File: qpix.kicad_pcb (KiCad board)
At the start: 2 copper layers, 82.6 x 93 mm, 113 parts, among them J1 Conn_01x32, J11 Conn_Coaxial_Power, J12 USB_A, J13 DigReset, J2 Conn_01x09, J3 TxRx_D, J4 TxRx_A, J5 SPI, J6 TxRx_B, J7 Conn_Coaxial, J8 TxRx_C, J9 Conn_Coaxial_Power, Q1 Q, Q2 Q, Q3 Q, Q4 Q, U1 qpix_digital, U2 TPS73101DBV, U3 9DMV0141AKILF, U4 DS90C401M_NOPB

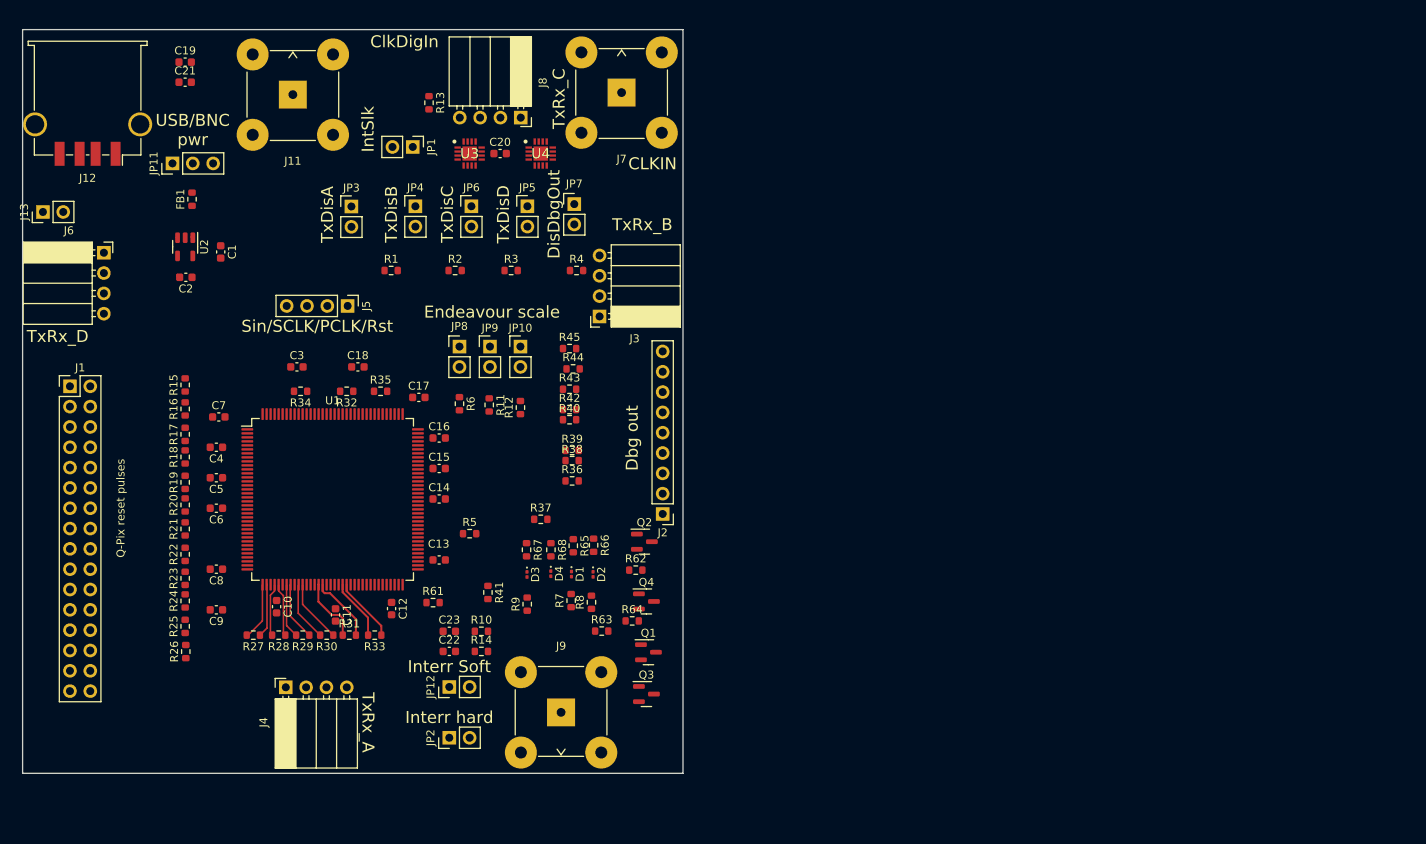
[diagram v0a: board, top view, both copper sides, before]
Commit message: add a footprint for QPix ASIC CoB  and its generator
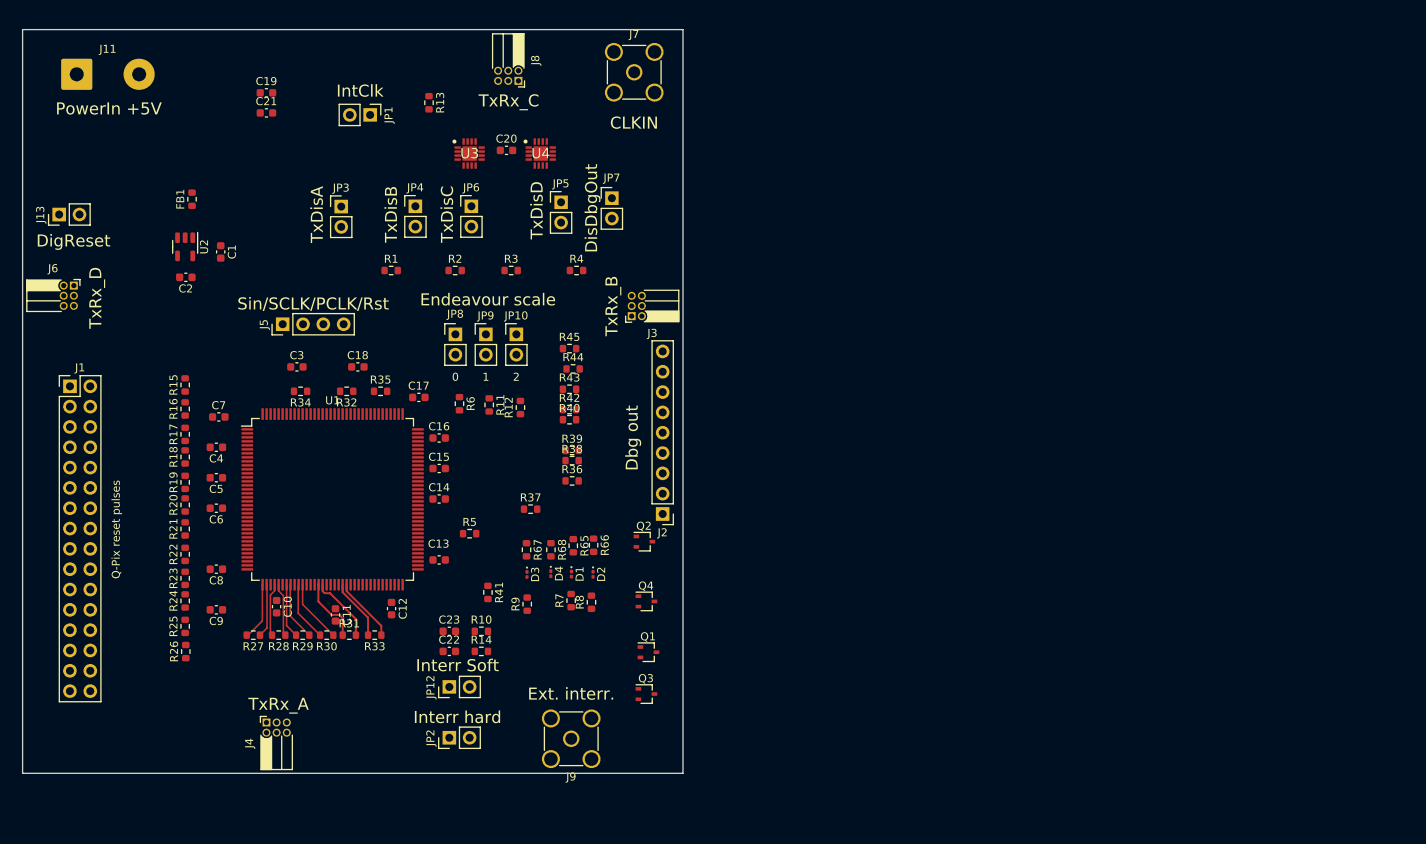
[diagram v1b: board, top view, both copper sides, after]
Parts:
- removed J12: USB_A, Connector_USB:USB_A_TE_292303-7_Horizontal
- removed JP11: , Connector_PinHeader_2.54mm:PinHeader_1x03_P2.54mm_Vertical
- removed R61, R62, R63, R64: 2.2k, Resistor_SMD:R_0603_1608Metric
- J11: footprint Connector_Coaxial:BNC_TEConnectivity_1478035_Horizontal -> Connector_Wire:SolderWire-1sqmm_1x02_P7.8mm_D1.4mm_OD3.9mm
- J3: value TxRx_D -> Conn_02x03; footprint Connector_PinSocket_2.54mm:PinSocket_1x04_P2.54mm_Horizontal -> Connector_PinSocket_1.27mm:PinSocket_2x03_P1.27mm_Horizontal
- J4: value TxRx_A -> Conn_02x03; footprint Connector_PinSocket_2.54mm:PinSocket_1x04_P2.54mm_Horizontal -> Connector_PinSocket_1.27mm:PinSocket_2x03_P1.27mm_Horizontal
- J6: value TxRx_B -> Conn_02x03; footprint Connector_PinSocket_2.54mm:PinSocket_1x04_P2.54mm_Horizontal -> Connector_PinSocket_1.27mm:PinSocket_2x03_P1.27mm_Horizontal
- J7, J9: footprint Connector_Coaxial:BNC_TEConnectivity_1478035_Horizontal -> Connector_Coaxial:SMA_Amphenol_901-144_Vertical
- J8: value TxRx_C -> Conn_02x03; footprint Connector_PinSocket_2.54mm:PinSocket_1x04_P2.54mm_Horizontal -> Connector_PinSocket_1.27mm:PinSocket_2x03_P1.27mm_Horizontal
- Q1, Q2, Q3, Q4: value Q -> Q_NMOS_GSD; footprint Package_TO_SOT_SMD:SOT-23 -> Package_TO_SOT_SMD:SOT-323_SC-70
- moved J11 27.1 mm to (102.0, 54.9)
- moved C19 10.9 mm to (125.7, 57.2)
- moved C21 10.9 mm to (125.7, 59.7)
- moved J5 8.43 mm to (127.8, 86.1), turned to 90 degrees
- moved JP1 6.66 mm to (138.7, 59.9)
- moved J6 5.56 mm to (101.7, 81.3)
- moved J4 5.02 mm to (125.7, 135.9)
- moved JP7 4.76 mm to (168.9, 70.4)
- moved J8 4.60 mm to (157.2, 55.7)
- moved JP5 4.24 mm to (162.6, 70.9)
- moved J3 4.02 mm to (171.4, 85.1)
- moved J9 3.54 mm to (163.8, 137.9)
- moved J7 2.99 mm to (171.7, 54.6)
- moved J13 2.06 mm to (99.8, 72.4)
- moved R37 1.80 mm to (158.8, 109.2)
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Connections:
- J11 pad 1: Net-(J11-Pad1) -> Net-(FB1-Pad2)
- J3 pad 2: Net-(J3-Pad2) -> Net-(U1-Pad106)
- J3 pad 3: Net-(J3-Pad3) -> GND
- J3 pad 4: Net-(J3-Pad4) -> GND
- J4 pad 2: Net-(J4-Pad2) -> Net-(U1-Pad54)
- J4 pad 3: Net-(J4-Pad3) -> GND
- J4 pad 4: Net-(J4-Pad4) -> GND
- J6 pad 2: Net-(J6-Pad2) -> Net-(U1-Pad62)
- J6 pad 3: Net-(J6-Pad3) -> GND
- J6 pad 4: Net-(J6-Pad4) -> GND
- J8 pad 2: Net-(J8-Pad2) -> Net-(U1-Pad101)
- J8 pad 3: Net-(J8-Pad3) -> GND
- J8 pad 4: Net-(J8-Pad4) -> GND
- Q1 pad 1: Net-(D1-Pad1) -> dbgClkDiv
- Q1 pad 2: Net-(R61-Pad2) -> GND
- Q1 pad 3: GND -> Net-(D1-Pad1)
- Q2 pad 1: Net-(D2-Pad1) -> dbgDataValid
- Q2 pad 2: Net-(Q2-Pad2) -> GND
- Q2 pad 3: GND -> Net-(D2-Pad1)
- Q3 pad 1: Net-(D3-Pad1) -> dbgRxValid
- Q3 pad 2: Net-(Q3-Pad2) -> GND
- Q3 pad 3: GND -> Net-(D3-Pad1)
- Q4 pad 1: Net-(D4-Pad1) -> dbgInterr
- Q4 pad 2: Net-(Q4-Pad2) -> GND
- Q4 pad 3: GND -> Net-(D4-Pad1)
- R31 pad 2: Net-(J4-Pad2) -> Net-(R31-Pad2)
- R32 pad 2: Net-(J3-Pad2) -> Net-(R32-Pad2)
- R33 pad 1: Net-(J6-Pad2) -> Net-(R33-Pad1)
- R35 pad 1: Net-(J8-Pad2) -> Net-(R35-Pad1)
- U1 pad 101: Net-(J8-Pad3) -> Net-(U1-Pad101)
- U1 pad 102: Net-(J8-Pad4) -> Net-(U1-Pad102)
- U1 pad 106: Net-(J3-Pad3) -> Net-(U1-Pad106)
- U1 pad 107: Net-(J3-Pad4) -> Net-(U1-Pad107)
- U1 pad 110: Net-(J3-Pad2) -> Net-(R32-Pad2)
- U1 pad 52: Net-(J4-Pad2) -> Net-(R31-Pad2)
- U1 pad 53: Net-(J4-Pad4) -> Net-(U1-Pad53)
- U1 pad 54: Net-(J4-Pad3) -> Net-(U1-Pad54)
- U1 pad 58: Net-(J6-Pad2) -> Net-(R33-Pad1)
- U1 pad 61: Net-(J6-Pad4) -> Net-(U1-Pad61)
- U1 pad 62: Net-(J6-Pad3) -> Net-(U1-Pad62)
- U1 pad 98: Net-(J8-Pad2) -> Net-(R35-Pad1)
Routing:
- net Net-(R31-Pad2): track 0.00 -> 8.42 mm
- net Net-(J4-Pad2): track 8.42 -> 0.00 mm
- net Net-(R33-Pad1): track 0.00 -> 8.10 mm
- net Net-(J6-Pad2): track 8.10 -> 0.00 mm
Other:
- board text added: "0"
- board text added: "1"
- board text added: "2"
- board text added: "DigReset"
- board text added: "Ext. interr."
- board text added: "IntClk"
- board text added: "PowerIn +5V"
- board text removed: "ClkDigIn"
- board text removed: "IntSlk"
- board text removed: "USB/BNC pwr"

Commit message: some changes
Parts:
- U1: footprint Package_QFP:TQFP-144_20x20mm_P0.5mm -> qpix-digi-pcb:qpix_digi_footprint
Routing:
- net (no net): track 0.00 -> 3.53 mm

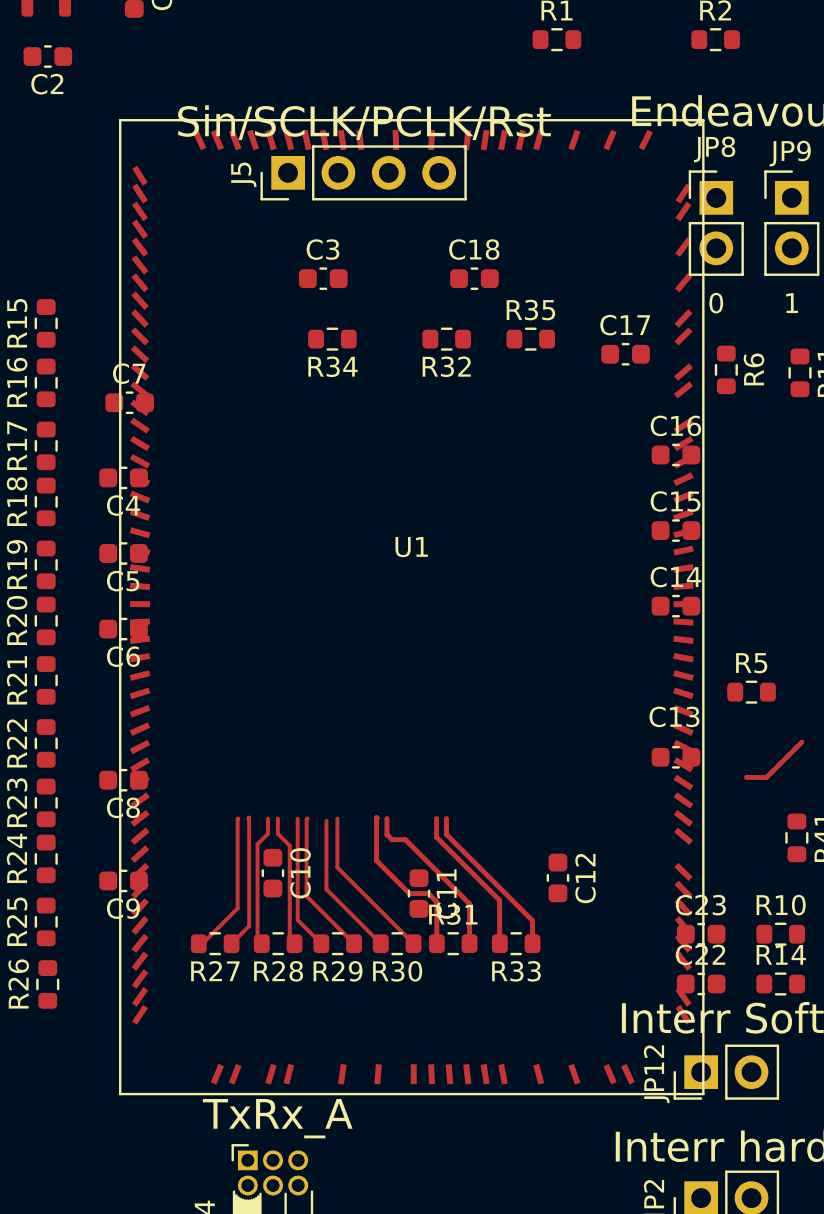
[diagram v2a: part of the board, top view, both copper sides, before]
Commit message: modify qpix footprint
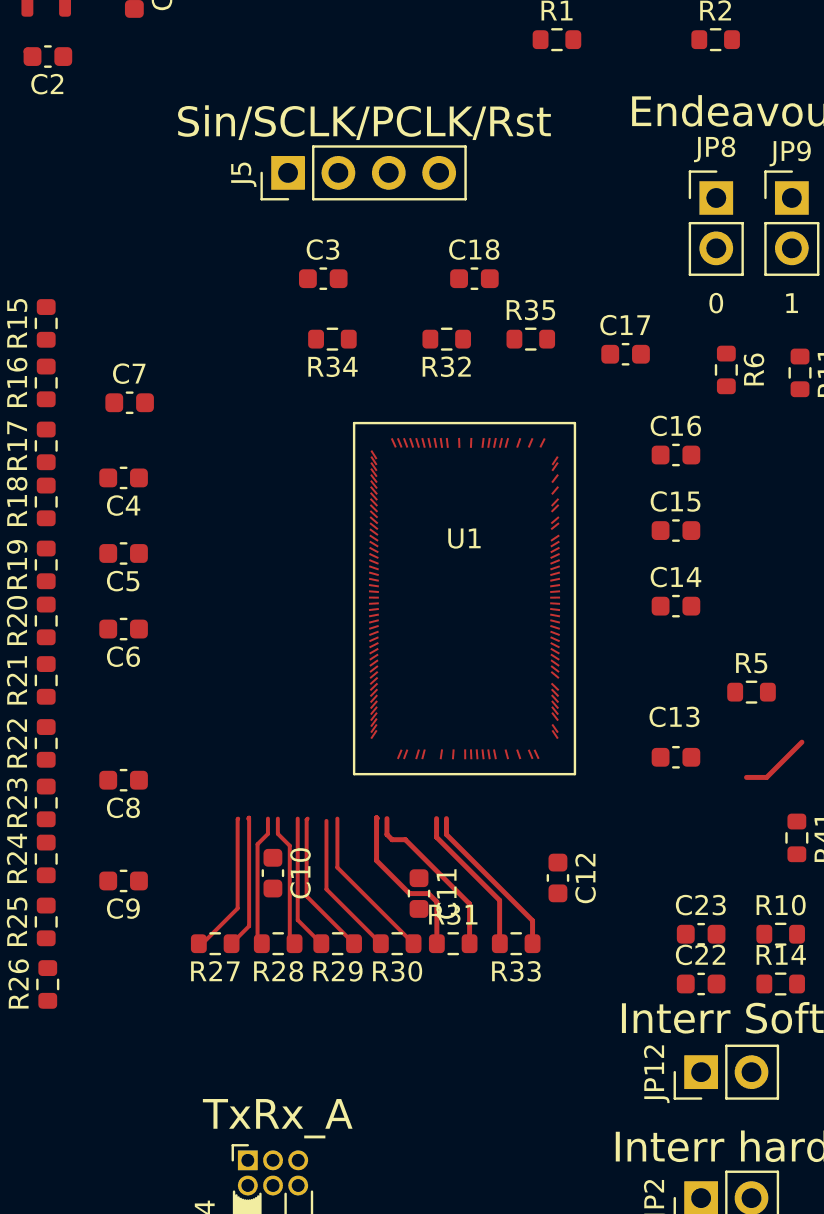
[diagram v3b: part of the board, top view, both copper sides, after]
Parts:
- moved U1 2.69 mm to (136.7, 107.6)

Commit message: some progress in routing
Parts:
- C12, C13, C14, C15, C16, C17, C18, C4, C5, C6, C7, C8, C9, R11, R12, R5, R6: moved to B.Cu
- moved D2 95.9 mm to (261.6, 129.9)
- moved R65 95.9 mm to (259.1, 126.4)
- moved R67 95.9 mm to (253.3, 126.9)
- moved D1 95.9 mm to (258.9, 129.9)
- moved D3 95.9 mm to (253.3, 130.0)
- moved D4 95.9 mm to (256.3, 129.9)
- moved R66 95.9 mm to (261.7, 126.3)
- moved R68 95.9 mm to (256.3, 126.9)
- moved Q1 94.0 mm to (267.4, 131.0)
- moved Q2 94.0 mm to (266.9, 117.2)
- moved Q3 94.0 mm to (267.1, 136.2)
- moved Q4 94.0 mm to (267.1, 124.6)
- moved R7 79.1 mm to (109.5, 63.1)
- moved R8 77.7 mm to (112.8, 64.5), turned to 0 degrees
- moved R9 71.5 mm to (115.8, 63.6)
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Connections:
- net Net-(JP1-Pad1) renamed /clkmux/SEL_AB
- net Net-(R31-Pad1) renamed /DatinA_P
- net Net-(R31-Pad2) renamed /DatinA_N
- net Net-(R33-Pad2) renamed /DatinB_P
- net Net-(U1-Pad53) renamed /DatoutA_N
- net Net-(U1-Pad54) renamed /DatoutA_P
- net Net-(U3-Pad15) renamed /clkmux/DO+
- net Net-(U3-Pad16) renamed /clkmux/DO-
- J6 pad 2: Net-(U1-Pad62) -> /DatinB_N
- J6 pad 5: Net-(U1-Pad61) -> /DatoutB_P
- J6 pad 6: Net-(R33-Pad1) -> /DatoutB_N
- R33 pad 1: Net-(R33-Pad1) -> /DatinB_N
- U1 pad 58: Net-(R33-Pad1) -> /DatinB_N
- U1 pad 61: Net-(U1-Pad61) -> /DatoutB_N
- U1 pad 62: Net-(U1-Pad62) -> /DatoutB_P
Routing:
- net /DatinB_N: track 0.00 -> 62.7 mm, vias 0 -> 2
- net /DatoutB_N: track 0.00 -> 55.2 mm, vias 0 -> 2
- net /DatoutB_P: track 0.00 -> 54.4 mm, vias 0 -> 2
- net /DatinB_P: track 7.63 -> 61.2 mm, vias 0 -> 2
- net Reset0_P: track 7.32 -> 56.5 mm
- net Reset1_P: track 6.80 -> 54.8 mm
- net Reset0_N: track 7.90 -> 53.7 mm
- net Reset1_N: track 7.32 -> 51.6 mm
- net VDD: track 0.00 -> 44.2 mm, vias 0 -> 27
- net GND: track 0.00 -> 44.2 mm, vias 0 -> 22
- net Reset4_P: track 0.00 -> 43.0 mm
- net Reset2_P: track 6.61 -> 48.6 mm
- net Reset5_P: track 0.00 -> 41.4 mm
- net Reset4_N: track 0.00 -> 41.2 mm
- net Reset6_P: track 0.00 -> 40.5 mm
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- added copper zone on In1.Cu, net GND
- added copper zone on In2.Cu, net VDD
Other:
- board size 82.6 x 93 mm -> 82.6 x 94.6 mm
- copper layers 2 -> 4
- board text added: "Power"
